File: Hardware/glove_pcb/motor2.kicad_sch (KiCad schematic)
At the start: 16 parts, among them J5 Conn_01x02, J6 Conn_01x02, U6 DRV8876PWPR, U7 DRV8876PWPR

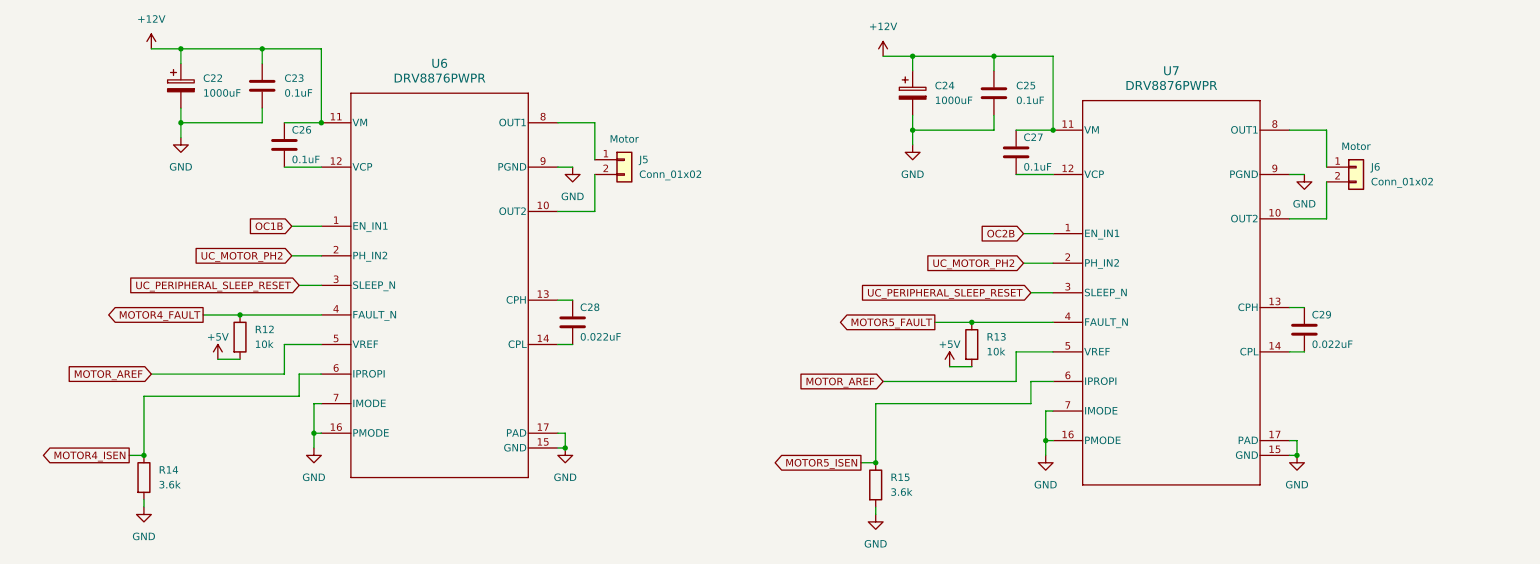
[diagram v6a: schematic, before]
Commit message: More updates to the schematic based on Dmitry's feedback
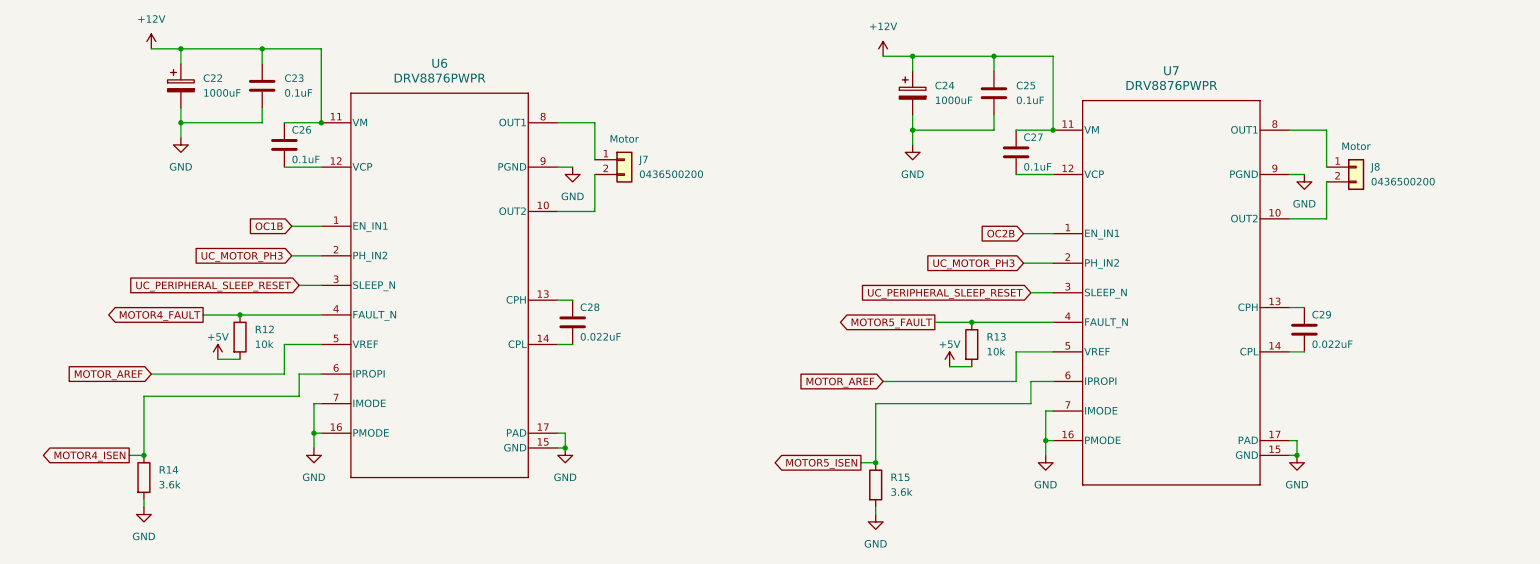
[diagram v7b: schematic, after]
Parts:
- J7: renamed from J5; value Conn_01x02 -> 0436500200
- J8: renamed from J6; value Conn_01x02 -> 0436500200
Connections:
- net UC_MOTOR_PH2 renamed UC_MOTOR_PH3
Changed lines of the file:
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@@
   (title_block
     (title "Motor Drivers (2/2)")
-    (date "2023-11-24")
+    (date "2024-01-24")
     (company "COEN 490 Team 15")
   )
@@
     )
   )
-  (global_label "UC_MOTOR_PH2" (shape input) (at 66.04 63.5 180) (fields_autoplaced)
+  (global_label "UC_MOTOR_PH3" (shape input) (at 66.04 63.5 180) (fields_autoplaced)
     (effects (font (size 1.27 1.27)) (justify right))
     (property "Intersheetrefs" "${INTERSHEET_REFS}" (at 48.3591 63.5 0)
@@
     )
   )
-  (global_label "UC_MOTOR_PH2" (shape input) (at 191.77 64.77 180) (fields_autoplaced)
+  (global_label "UC_MOTOR_PH3" (shape input) (at 191.77 64.77 180) (fields_autoplaced)
     (effects (font (size 1.27 1.27)) (justify right))
     (property "Intersheetrefs" "${INTERSHEET_REFS}" (at 174.0891 64.77 0)
@@
   (symbol (lib_id "Connector_Generic:Conn_01x02") (at 248.92 48.26 0) (unit 1)
     (in_bom yes) (on_board yes) (dnp no) (fields_autoplaced)
-    (property "Reference" "J6" (at 251.46 48.26 0)
+    (property "Reference" "J8" (at 251.46 48.26 0)
       (effects (font (size 1.27 1.27)) (justify left))
     )
-    (property "Value" "Conn_01x02" (at 251.46 50.8 0)
+    (property "Value" "0436500200" (at 251.46 50.8 0)
       (effects (font (size 1.27 1.27)) (justify left))
     )
@@
       (project "glove_pcb"
         (path "/747ff5f3-d342-40b0-8e4e-75b3a3063e75/244d4343-af6d-4477-97fd-05de712328be"
-          (reference "J6") (unit 1)
+          (reference "J8") (unit 1)
         )
       )
@@
   (symbol (lib_id "Connector_Generic:Conn_01x02") (at 123.19 46.99 0) (unit 1)
     (in_bom yes) (on_board yes) (dnp no) (fields_autoplaced)
-    (property "Reference" "J5" (at 125.73 46.99 0)
+    (property "Reference" "J7" (at 125.73 46.99 0)
       (effects (font (size 1.27 1.27)) (justify left))
     )
-    (property "Value" "Conn_01x02" (at 125.73 49.53 0)
+    (property "Value" "0436500200" (at 125.73 49.53 0)
       (effects (font (size 1.27 1.27)) (justify left))
     )
@@
       (project "glove_pcb"
         (path "/747ff5f3-d342-40b0-8e4e-75b3a3063e75/244d4343-af6d-4477-97fd-05de712328be"
-          (reference "J5") (unit 1)
+          (reference "J7") (unit 1)
         )
       )

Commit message: Change isp pin symbol
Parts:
- U6, U7: footprint PWP0016J_N -> Glove_Footprints:PWP0016J_N
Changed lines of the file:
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@@
       (effects (font (size 1.524 1.524)))
     )
-    (property "Footprint" "PWP0016J_N" (at 217.17 69.85 0)
+    (property "Footprint" "Glove_Footprints:PWP0016J_N" (at 217.17 69.85 0)
       (effects (font (size 1.27 1.27) italic) hide)
     )
@@
       (effects (font (size 1.524 1.524)))
     )
-    (property "Footprint" "PWP0016J_N" (at 91.44 68.58 0)
+    (property "Footprint" "Glove_Footprints:PWP0016J_N" (at 91.44 68.58 0)
       (effects (font (size 1.27 1.27) italic) hide)
     )
